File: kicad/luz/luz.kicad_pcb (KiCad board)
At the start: 4 copper layers, 53.1 x 30 mm, 89 parts, among them J2 U261-241N-4BS60, J3 Screw_Terminal_01x05, Q1 AO3400A, Q2 AO3400A, Q3 AO3400A, Q4 AO3400A, Q5 AOD413A, U1 STUSB4500QTR, U2 ESP32-S3, U3 W25Q16JVSSIQ, U4 SPX3819M5-L-3-3, Y1 40MHz

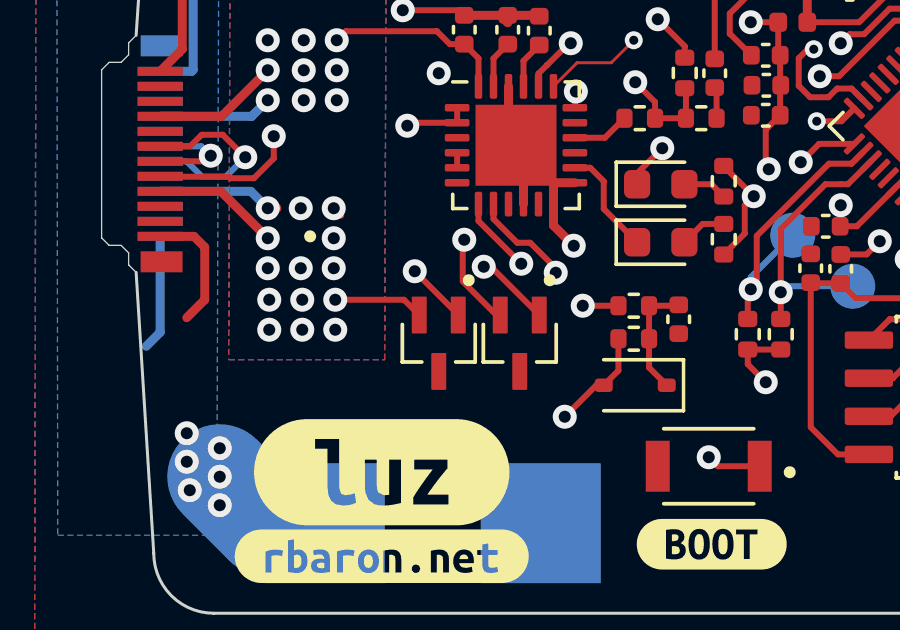
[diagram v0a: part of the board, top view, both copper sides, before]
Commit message: Route DISCH pin through 1k resistor
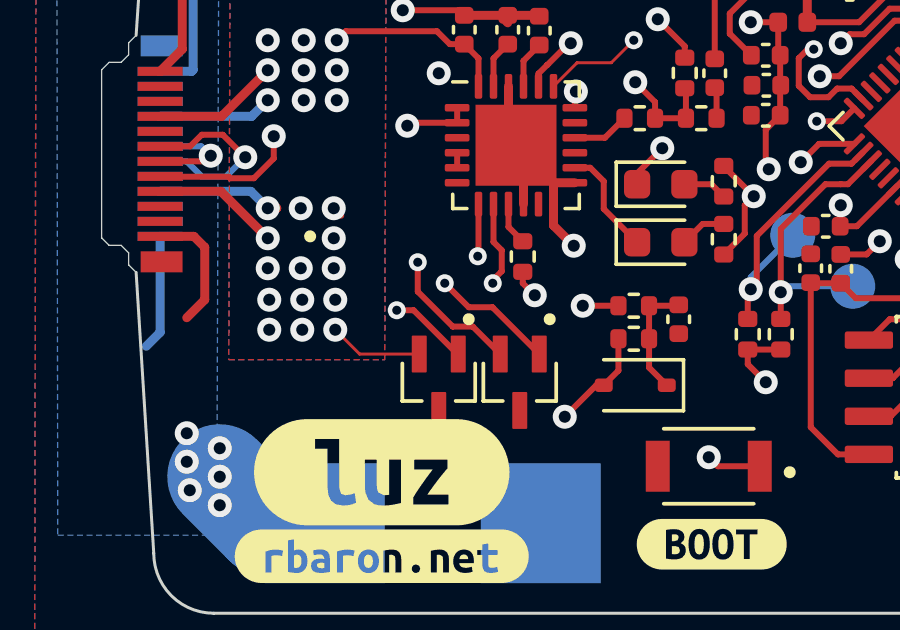
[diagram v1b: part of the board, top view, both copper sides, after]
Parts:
- added R15: 1k, Resistor_SMD:R_0402_1005Metric, F.Cu at (67.3, 103.1)
- moved D1 1.30 mm to (67.2, 107.3)
- moved D2 1.30 mm to (64.5, 107.3)
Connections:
- U1 pad 9: unconnected-(U1-DISCH-Pad9) -> Net-(U1-DISCH)
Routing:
- net USBD+: track 35.3 -> 39.8 mm
- net USBD-: track 36.4 -> 40.7 mm
- net SDA: track 20.8 -> 24.5 mm
- net SCL: track 20.9 -> 24.3 mm
- net CC1: track 18.6 -> 21.1 mm
- net Net-(U1-DISCH): track 0.00 -> 1.43 mm
- net +12V: track 10.0 -> 11.0 mm, vias 25 -> 26

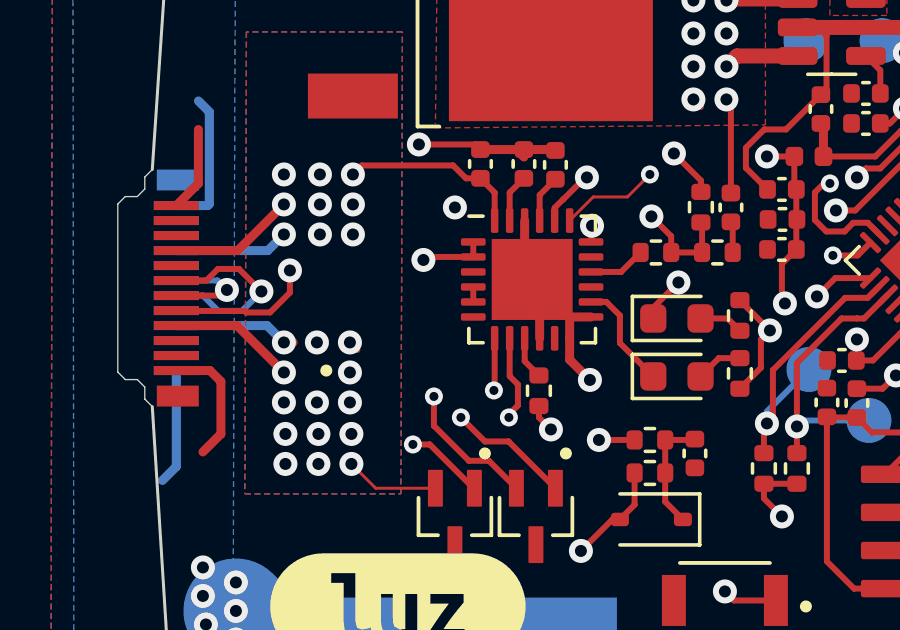
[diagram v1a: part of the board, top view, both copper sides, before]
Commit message: Pull down RST from STUSB45, as suggested by datasheet
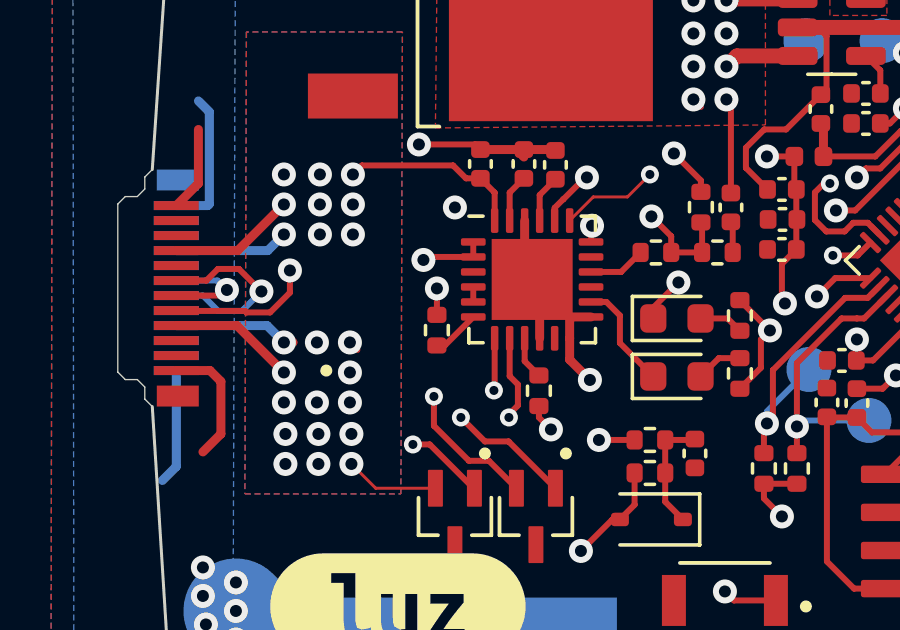
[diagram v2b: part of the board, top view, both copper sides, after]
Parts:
- added R16: 10k, Resistor_SMD:R_0402_1005Metric, F.Cu at (63.9, 101.1)
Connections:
- U1 pad 6: unconnected-(U1-RESET-Pad6) -> Net-(U1-RESET)
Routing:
- net Net-(U1-RESET): track 0.00 -> 1.61 mm
- net GND: track 66.4 -> 67.3 mm, vias 33 -> 34

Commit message: Connect shield
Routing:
- net unconnected-(J2-SHIELD-PadSH1): track 0.00 -> 13.4 mm, vias 0 -> 2
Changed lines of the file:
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@@
   (segment (start 56.2625 96.93706) (end 56.3125 96.88706) (width 0.3) (layer "B.Cu") (net 2))
   (segment (start 58.75 112) (end 57.2 110.45) (width 3.5) (layer "B.Cu") (net 2))
-  (segment (start 55.2125 105.6375) (end 54.75 106.1) (width 0.3) (layer "B.Cu") (net 2))
-  (segment (start 55.2125 102.43706) (end 55.2125 105.6375) (width 0.3) (layer "B.Cu") (net 2))
+  (segment (start 56.8 102.7) (end 56.8 104.5) (width 0.3) (layer "B.Cu") (net 2))
+  (segment (start 55.2125 102.43706) (end 56.53706 102.43706) (width 0.3) (layer "B.Cu") (net 2))
   (segment (start 56.3125 96.88706) (end 56.3125 93.8125) (width 0.3) (layer "B.Cu") (net 2))
   (segment (start 88.9 91.44) (end 88.9 92.6) (width 0.2) (layer "B.Cu") (net 2))
@@
   (segment (start 55.2125 96.93706) (end 56.2625 96.93706) (width 0.3) (layer "B.Cu") (net 2))
   (segment (start 88.9 92.6) (end 88.1 93.4) (width 0.2) (layer "B.Cu") (net 2))
+  (segment (start 56.8 104.5) (end 56.3 105) (width 0.3) (layer "B.Cu") (net 2))
+  (segment (start 56.53706 102.43706) (end 56.8 102.7) (width 0.3) (layer "B.Cu") (net 2))
   (segment (start 78.2 95.7) (end 77.9 96) (width 0.2) (layer "F.Cu") (net 3))
   (segment (start 80.689168 94.847911) (end 79.530029 94.847911) (width 0.2) (layer "F.Cu") (net 3))
@@
   (segment (start 55.2125 98.43706) (end 58.26294 98.43706) (width 0.3) (layer "B.Cu") (net 53))
   (segment (start 58.26294 98.43706) (end 58.8 97.9) (width 0.3) (layer "B.Cu") (net 53))
+  (segment (start 55.2625 103.28706) (end 55.2625 104.7375) (width 0.2) (layer "F.Cu") (net 54))
+  (segment (start 55.2625 104.7375) (end 55.1 104.9) (width 0.2) (layer "F.Cu") (net 54))
+  (via (at 55 94.7) (size 0.6) (drill 0.3) (layers "F.Cu" "B.Cu") (net 54))
+  (via (at 55.1 104.9) (size 0.6) (drill 0.3) (layers "F.Cu" "B.Cu") (net 54))
+  (segment (start 55 94.7) (end 55 104.8) (width 0.2) (layer "In1.Cu") (net 54))
+  (segment (start 55 104.8) (end 55.1 104.9) (width 0.2) (layer "In1.Cu") (net 54))
+  (segment (start 55.2625 94.9625) (end 55 94.7) (width 0.2) (layer "B.Cu") (net 54))
+  (segment (start 55.2625 96.08706) (end 55.2625 94.9625) (width 0.2) (layer "B.Cu") (net 54))
   (segment (start 78.68 93.2) (end 78.68 92.43) (width 0.2) (layer "F.Cu") (net 66))
   (segment (start 78.68 92.43) (end 78.2 91.95) (width 0.2) (layer "F.Cu") (net 66))

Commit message: Plotted files for production
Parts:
- removed kibuzzard-6551FE7F: G***, kibuzzard-6551FE7F
- added kibuzzard-65527C49: G***, kibuzzard-65527C49, F.Cu at (62.6, 110.9)
- moved kibuzzard-6551FE89 0.30 mm to (62.6, 113.4)

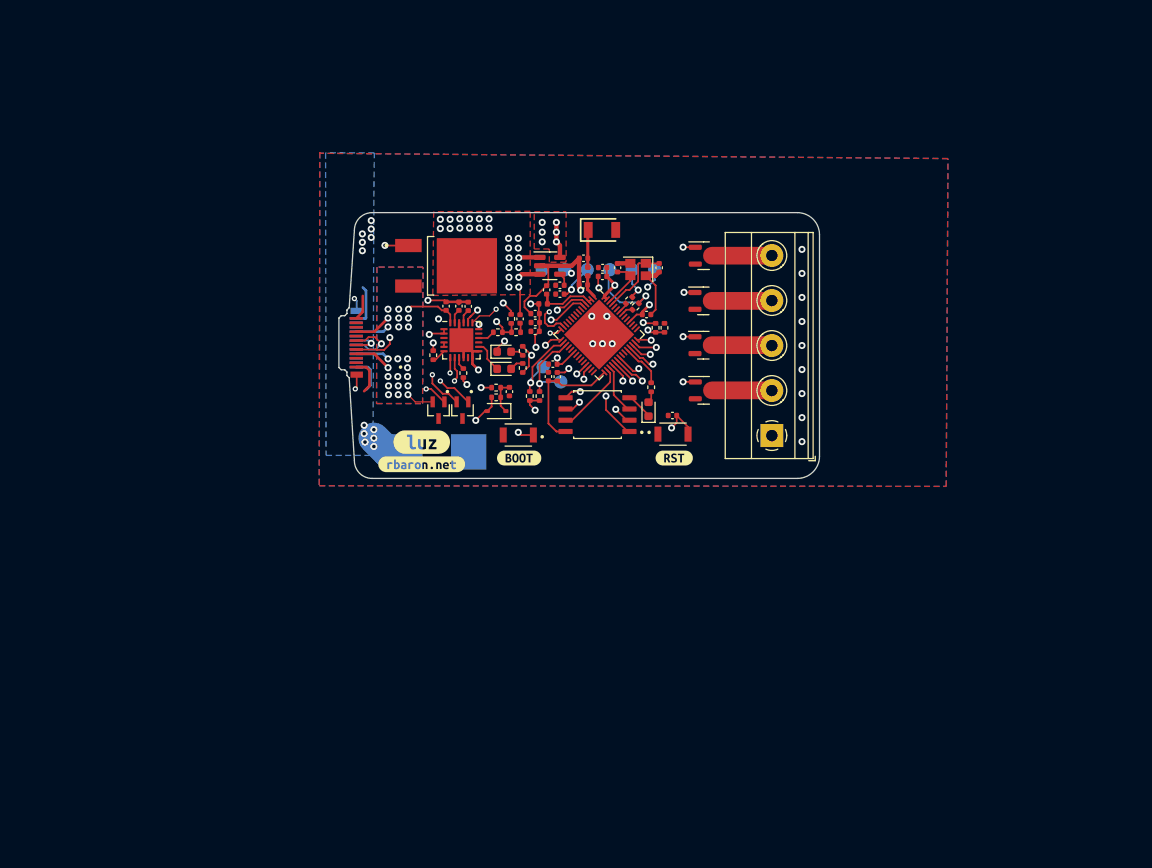
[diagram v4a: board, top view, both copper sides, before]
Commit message: Routed new version with ESP32-WROOM
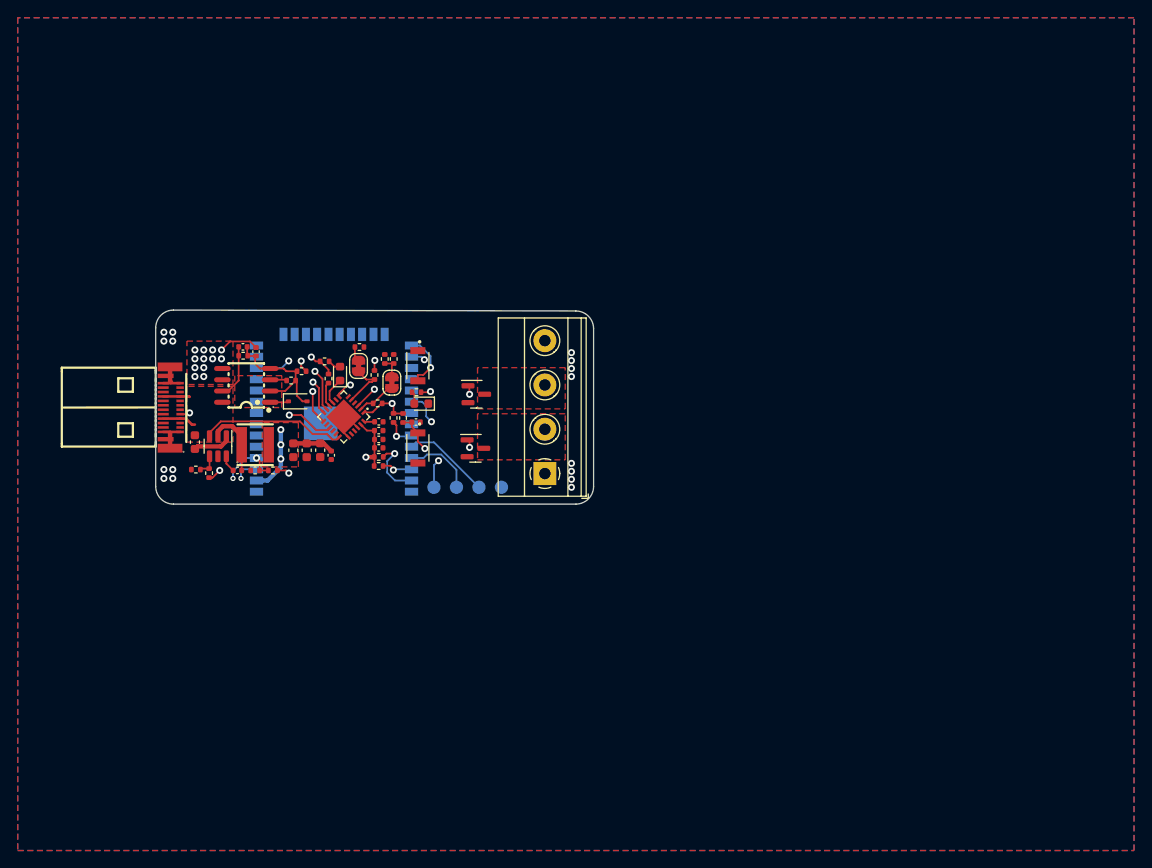
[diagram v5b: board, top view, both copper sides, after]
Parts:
- removed ANT1: ANT3216LL00R2400A, Snapeda:ANTC3216X135N
- removed C13, C14, C16, C20: 1u, Capacitor_SMD:C_0402_1005Metric
- removed C15: 10n, Capacitor_SMD:C_0402_1005Metric
- removed C17, C18, C19: 100n, Capacitor_SMD:C_0402_1005Metric
- removed C21: 10u, Capacitor_SMD:C_0402_1005Metric
- removed D2: ESDA25W, Snapeda:SOT65P210X110-3N
- removed D5: 1N5819WS, Diode_SMD:D_SOD-323
- removed D6: PO3, LED_SMD:LED_0603_1608Metric
- removed J3: Screw_Terminal_01x05, TerminalBlock_Phoenix:TerminalBlock_Phoenix_MKDS-1,5-5-5.08_1x05_P5.08mm_Horizontal
- removed L2: 2.2n, Inductor_SMD:L_0402_1005Metric
- removed Q2, Q3: AO3400A, Package_TO_SOT_SMD:SOT-23
- removed Q5: AOD413A, Snapeda:TRANS_AOD413A
- removed R13, R14: 470, Resistor_SMD:R_0402_1005Metric
- removed TP1, TP10, TP6, TP9: TestPoint, TestPoint:TestPoint_Pad_D1.5mm
- removed TP7, TP8: TestPoint, TestPoint:TestPoint_Pad_4.0x4.0mm
- removed Y1: 40MHz, Crystal:Crystal_SMD_2520-4Pin_2.5x2.0mm
- removed kibuzzard-6551E21C: G***, kibuzzard-6551E21C
- removed kibuzzard-6551E233: G***, kibuzzard-6551E233
- removed kibuzzard-6551E248: G***, kibuzzard-6551E248
- removed kibuzzard-6551E256: G***, kibuzzard-6551E256
- removed kibuzzard-6551FCCC: G***, kibuzzard-6551FCCC
- removed kibuzzard-6551FD82: G***, kibuzzard-6551FD82
- removed kibuzzard-6551FDB9: G***, kibuzzard-6551FDB9
- removed kibuzzard-6551FDF9: G***, kibuzzard-6551FDF9
- removed kibuzzard-6551FE00: G***, kibuzzard-6551FE00
- removed kibuzzard-6551FE06: G***, kibuzzard-6551FE06
- removed kibuzzard-6551FE0C: G***, kibuzzard-6551FE0C
- removed kibuzzard-6551FE14: G***, kibuzzard-6551FE14
- removed kibuzzard-6551FE1B: G***, kibuzzard-6551FE1B
- removed kibuzzard-6551FE21: G***, kibuzzard-6551FE21
- removed kibuzzard-6551FE26: G***, kibuzzard-6551FE26
- removed kibuzzard-6551FE89: G***, kibuzzard-6551FE89
- removed kibuzzard-65520027: G***, kibuzzard-65520027
- removed kibuzzard-65522F33: G***, kibuzzard-65522F33
- removed kibuzzard-65522F45: G***, kibuzzard-65522F45
- removed kibuzzard-65527C49: G***, kibuzzard-65527C49
- added JP1: 12V, Jumper:SolderJumper-2_P1.3mm_Bridged_RoundedPad1.0x1.5mm, F.Cu at (59.2, 104.2)
- added JP2: 3A/5A, Jumper:SolderJumper-2_P1.3mm_Bridged_RoundedPad1.0x1.5mm, F.Cu at (55.5, 102.3)
- added R17: 10k, Resistor_SMD:R_0402_1005Metric, F.Cu at (57.6, 106.5)
- added R18: 10k, Resistor_SMD:R_0402_1005Metric, F.Cu at (59.4, 101.5)
- added R19: 10k, Resistor_SMD:R_0402_1005Metric, F.Cu at (58.4, 101.5)
- added R21: 10k, Resistor_SMD:R_0402_1005Metric, F.Cu at (57.3, 103.3)
- added R22: 10k, Resistor_SMD:R_0402_1005Metric, F.Cu at (55.6, 100.2)
- added U5: ESP32-WROOM-32D, RF_Module:ESP32-WROOM-32D, B.Cu at (52.7, 108.3)
- C1, C10: value 100n -> 1u
- C12, C2: value 1u -> 10u; footprint Capacitor_SMD:C_0402_1005Metric -> Capacitor_SMD:C_0603_1608Metric
- C3: value 100n -> 10u; footprint Capacitor_SMD:C_0402_1005Metric -> Capacitor_SMD:C_0603_1608Metric
- C4: value 10p -> 1u
- C5: value 10p -> 100n
- C6: value 5.1p -> 100n
- C7: value 3.9p -> 1u
- C9: footprint Capacitor_SMD:C_0402_1005Metric -> Capacitor_SMD:C_0603_1608Metric
- D1: value ESDA25W -> PO3; footprint Snapeda:SOT65P210X110-3N -> LED_SMD:LED_0603_1608Metric
- D3: value PO2 -> 15V; footprint LED_SMD:LED_0603_1608Metric -> Diode_SMD:D_SOD-323
- J2: value U261-241N-4BS60 -> Screw_Terminal_01x04; footprint Snapeda:XKB_U261-241N-4BS60 -> TerminalBlock_Phoenix:TerminalBlock_Phoenix_MKDS-1,5-4_1x04_P5.00mm_Horizontal
- L1: value 2.2n -> SWPA4030S470MT; footprint Inductor_SMD:L_0402_1005Metric -> footprint:IND-SMD_L4.0-W4.0_SLS3DXX
- R1: value 22k -> 1k
- R10: value 1k -> 100k
- R16: value 10k -> 22k
- R2: value 100k -> 10k
- R3: value 100 -> 1k
- R4: value 1k -> 47k
- R7: value 470 -> 4.7k
- S1: value B3U-1000P -> BOOT
- S2: value B3U-1000P -> RST
- U1: value STUSB4500QTR -> U261-241N-4BS2SS; footprint Package_DFN_QFN:QFN-24-1EP_4x4mm_P0.5mm_EP2.7x2.7mm -> footprint:USB-C-SMD_U261-241N-4BS2SS
- U2: value ESP32-S3 -> CYPD3177-24LQXQ_C2959321; footprint Package_DFN_QFN:QFN-56-1EP_7x7mm_P0.4mm_EP5.6x5.6mm -> footprint:TQFN-24_L4.0-W4.0-P0.50-TL-EP2.8
- U3: value W25Q16JVSSIQ -> ~; footprint Snapeda:SOIC127P790X216-8N -> footprint:SO-8_L4.9-W3.9-P1.27-LS5.9-BL
- U4: value SPX3819M5-L-3-3 -> TPS54302; footprint Package_TO_SOT_SMD:SOT-23-5 -> Package_TO_SOT_SMD:SOT-23-6
- moved R10 50.8 mm to (38.6, 114.4)
- moved R12 48.9 mm to (43.8, 114.1), turned to 0 degrees
- moved R11 46.1 mm to (45.8, 114.1), turned to 0 degrees
- moved U4 42.6 mm to (39.6, 111.4), turned to -90 degrees
- moved L1 42.3 mm to (43.8, 111.2), turned to 0 degrees
- moved C8 42.0 mm to (41.8, 114.1)
- moved C2 41.6 mm to (37.0, 110.9), turned to 90 degrees
- moved C3 39.9 mm to (51.1, 111.8), turned to 90 degrees
- moved U3 39.8 mm to (42.8, 104.5), turned to 90 degrees
- moved C4 37.1 mm to (57.8, 110.6), turned to 0 degrees
- moved C9 33.6 mm to (49.6, 111.8), turned to 90 degrees
- moved U1 33.6 mm to (34.4, 107.0), turned to -90 degrees
- moved C5 32.6 mm to (57.8, 109.6), turned to 0 degrees
- moved C10 31.4 mm to (42.4, 100.2), turned to 0 degrees
- moved R2 30.5 mm to (42.5, 101.2), turned to 180 degrees
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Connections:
- C1 pad 1: VDD_SPI -> GND
- C1 pad 2: GND -> Net-(U5-EN)
- C10 pad 1: +12V -> VBUS
- C10 pad 2: Net-(C10-Pad2) -> Net-(D3-A)
- C11 pad 1: Net-(U1-VREG_2V7) -> VDCOUT
- C11 pad 2: GND -> Net-(D3-A)
- C12 pad 1: Net-(U1-VREG_1V2) -> GND
- C12 pad 2: GND -> +3V3
- C2 pad 2: VDD_SPI -> VBUS
- C3 pad 2: Net-(U2-CHIP_PU/RESET) -> +3V3
- C4 pad 1: GND -> +3V3
- C4 pad 2: Net-(U2-XTAL_N) -> GND
- C5 pad 1: GND -> +3V3
- C5 pad 2: Net-(U2-XTAL_P) -> GND
- C6 pad 1: GND -> +3V3
- C6 pad 2: LNA_IN -> GND
- C7 pad 1: GND -> Net-(U2-VCCD)
- C7 pad 2: Net-(ANT1-FEED) -> GND
- C8 pad 1: GND -> Net-(U4-BOOT)
- C8 pad 2: Net-(U4-BP) -> Net-(U4-SW)
- D1 pad 1: USBD+ -> GND
- D1 pad 2: USBD- -> Net-(D1-A)
- D3 pad 1: Net-(D3-K) -> FETs
- L1 pad 1: LNA_IN -> Net-(U4-SW)
- L1 pad 2: Net-(ANT1-FEED) -> +3V3
- Q1 pad 3: Net-(J3-Pin_3) -> Net-(J2-Pin_3)
- Q4 pad 3: Net-(J3-Pin_2) -> Net-(J2-Pin_2)
- R1 pad 1: Net-(U1-VBUS_EN_SNK) -> +3V3
- R1 pad 2: Net-(Q5-Pad1) -> Net-(U2-FLIP)
- R10 pad 1: Net-(U2-GPIO33) -> Net-(U4-FB)
- R10 pad 2: Net-(D6-A) -> +3V3
- R11 pad 2: +12V -> VDCOUT
- R15 pad 1: +12V -> Net-(U5-IO27)
- R15 pad 2: Net-(U1-DISCH) -> Net-(D1-A)
- R16 pad 1: Net-(U1-RESET) -> GND
- R16 pad 2: GND -> Net-(U4-FB)
- R2 pad 1: Net-(Q5-Pad1) -> Net-(D3-A)
- R3 pad 1: Net-(C10-Pad2) -> Net-(D3-A)
- R3 pad 2: Net-(Q5-Pad1) -> VBUS_EN
- R4 pad 1: +3V3 -> FETs
- R6 pad 1: Net-(U1-VBUS_VS_DISCH) -> +3V3
- R6 pad 2: Net-(D5-K) -> Net-(U5-EN)
- R7 pad 1: VBUS -> HPIINT
- R7 pad 2: Net-(D5-K) -> +3V3
- R8 pad 2: SCL -> SDA
- R9 pad 1: SDA -> SCL
- S1 pad 2: Net-(U2-CHIP_PU/RESET) -> Net-(U5-IO0)
- S2 pad 1: Net-(U2-GPIO0/BOOT) -> Net-(U5-EN)
- U2 pad 1: LNA_IN -> +3V3
- U2 pad 10: unconnected-(U2-GPIO5/ADC1_CH4-Pad10) -> Net-(U2-FLIP)
- U2 pad 11: unconnected-(U2-GPIO6/ADC1_CH5-Pad11) -> VDCOUT
- U2 pad 12: unconnected-(U2-GPIO7/ADC1_CH6-Pad12) -> SDA
- U2 pad 13: ALERT -> SCL
- U2 pad 14: VMon -> unconnected-(U2-CC2-Pad14)
- U2 pad 15: G10 -> CC1
- U2 pad 16: SCL -> unconnected-(U2-D--Pad16)
- U2 pad 17: SDA -> unconnected-(U2-D+-Pad17)
- U2 pad 18: unconnected-(U2-GPIO13/ADC2_CH2-Pad18) -> VBUS
- U2 pad 19: unconnected-(U2-GPIO14/ADC2_CH3-Pad19) -> GND
- U2 pad 2: VDD3P3 -> VBMAX
- U2 pad 20: +3V3 -> unconnected-(U2-DNU1-Pad20)
- U2 pad 22: unconnected-(U2-GPIO16/ADC2_CH5/XTAL_32K_N-Pad22) -> GND
- U2 pad 23: unconnected-(U2-GPIO17/ADC2_CH6-Pad23) -> +3V3
- U2 pad 24: unconnected-(U2-GPIO18/ADC2_CH7-Pad24) -> Net-(U2-VCCD)
- U2 pad 25: USBD- -> GND
- U2 pad 3: VDD3P3 -> VBUS_EN
- U2 pad 4: Net-(U2-CHIP_PU/RESET) -> unconnected-(U2-SAFE_PWR_EN-Pad4)
- U2 pad 5: Net-(U2-GPIO0/BOOT) -> ICOA
- U2 pad 6: unconnected-(U2-GPIO1/ADC1_CH0-Pad6) -> GND
- U2 pad 7: unconnected-(U2-GPIO2/ADC1_CH1-Pad7) -> HPIINT
- U2 pad 9: unconnected-(U2-GPIO4/ADC1_CH3-Pad9) -> Net-(D4-K)
- U3 pad 1: SPICS -> FETs
- U3 pad 2: SPIQ -> Net-(D3-A)
- U3 pad 3: SPIWP -> FETs
- U3 pad 4: GND -> Net-(D3-A)
- U3 pad 5: SPID -> VDCOUT
- U3 pad 6: SPICLK -> VDCOUT
- U3 pad 7: SPIHD -> VBUS
- U3 pad 8: VDD_SPI -> VBUS
- U4 pad 1: +12V -> GND
- U4 pad 2: GND -> Net-(U4-SW)
- U4 pad 3: +12V -> VBUS
- U4 pad 4: Net-(U4-BP) -> Net-(U4-FB)
- U4 pad 5: +3V3 -> unconnected-(U4-EN-Pad5)
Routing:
- net GND: track 67.6 -> 16.4 mm, vias 34 -> 16
- net USBD-: track 40.7 -> 0.00 mm, vias 3 -> 0
- net USBD+: track 39.8 -> 0.00 mm, vias 3 -> 0
- net Net-(U5-EN): track 0.00 -> 31.3 mm, vias 0 -> 2
- net Net-(U2-CHIP_PU/RESET): track 27.6 -> 0.00 mm, vias 2 -> 0
- net Net-(U5-IO27): track 0.00 -> 23.4 mm, vias 0 -> 2
- net Net-(Q5-Pad1): track 22.4 -> 0.00 mm, vias 2 -> 0
- net VBUS: track 51.1 -> 29.5 mm, vias 25 -> 0
- net Net-(U2-GPIO0/BOOT): track 20.7 -> 0.00 mm, vias 2 -> 0
- net HPIINT: track 0.00 -> 20.0 mm, vias 0 -> 2
- net C4: track 14.9 -> 0.00 mm, vias 2 -> 0
- net VDD_SPI: track 14.3 -> 0.00 mm
- net Net-(D3-A): track 1.48 -> 15.6 mm
- net VBUS_EN: track 0.00 -> 13.6 mm, vias 0 -> 2
- net ALERT: track 13.6 -> 0.00 mm, vias 2 -> 0
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- added copper zone on F.Cu, net FETs
- added copper zone on F.Cu, net Net-(J2-Pin_2)
- added copper zone on F.Cu, net Net-(J2-Pin_3)
- added copper zone on F.Cu, net VDCOUT
- added copper zone on In1.Cu, net VDCOUT
- removed copper zone on B.Cu, net +12V
- removed copper zone on F.Cu, net +12V
- removed copper zone on In1.Cu, net GND
- removed copper zone on B.Cu, net VBUS
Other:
- board size 53.1 x 30 mm -> 49.4 x 21.9 mm

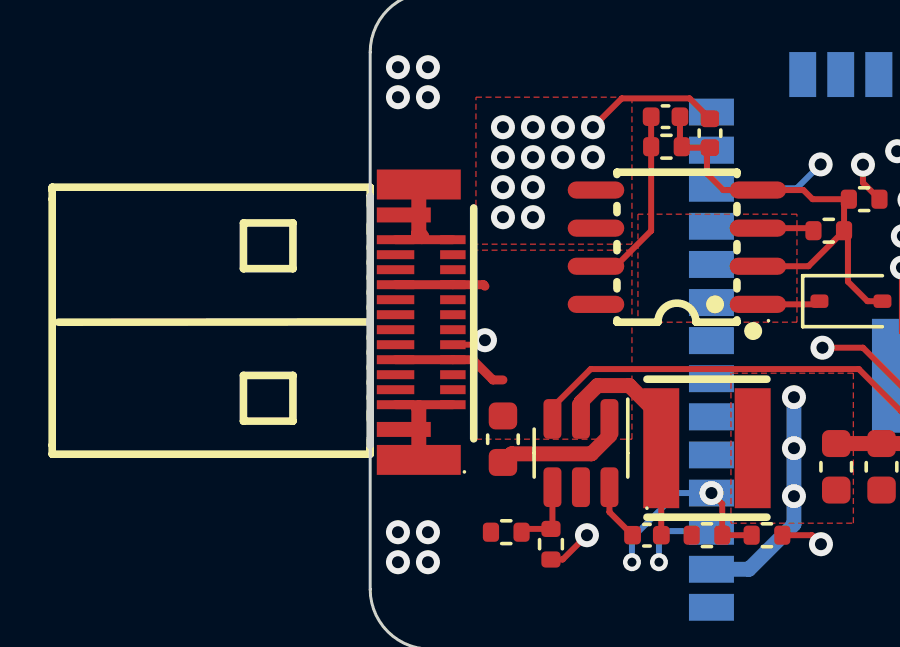
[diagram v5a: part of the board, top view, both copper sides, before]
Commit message: Better ground plane
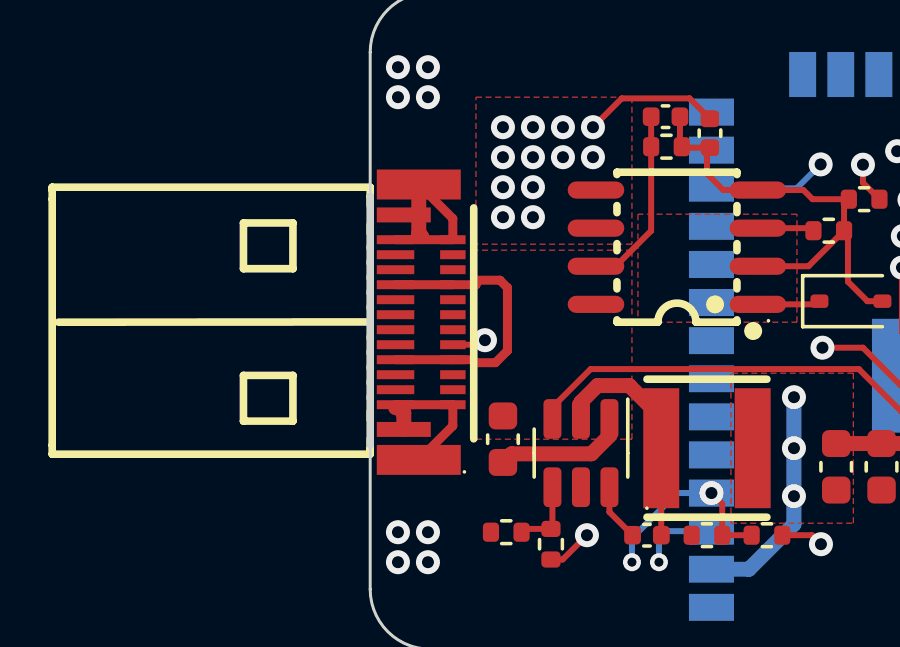
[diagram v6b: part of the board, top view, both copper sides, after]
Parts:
- added kibuzzard-655BB076: G***, kibuzzard-655BB076, B.Cu at (64.0, 114.2)
- added kibuzzard-655BB09E: G***, kibuzzard-655BB09E, B.Cu at (66.5, 114.2)
- added kibuzzard-655BB0B1: G***, kibuzzard-655BB0B1, B.Cu at (69.1, 114.2)
- added kibuzzard-655BB0BF: G***, kibuzzard-655BB0BF, B.Cu at (71.6, 114.2)
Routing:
- net GND: track 16.4 -> 20.2 mm
- net VBUS: track 29.5 -> 32.2 mm
